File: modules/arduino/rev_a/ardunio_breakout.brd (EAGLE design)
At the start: 68.6 x 66 mm, 2 parts, among them J1 MODULE_GENERIC, U1 ARDUINO_SHIELDLABEL

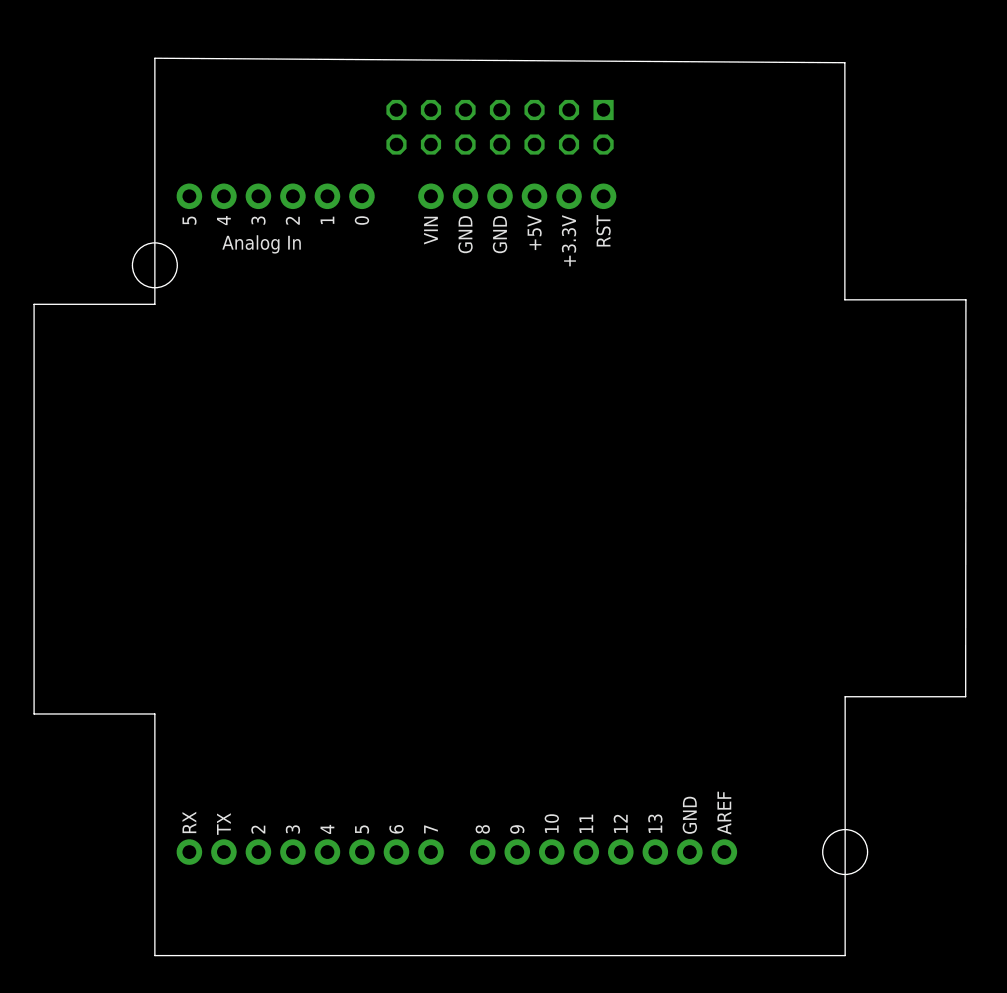
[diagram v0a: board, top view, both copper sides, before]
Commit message: Arduino Module: Regulator and headers
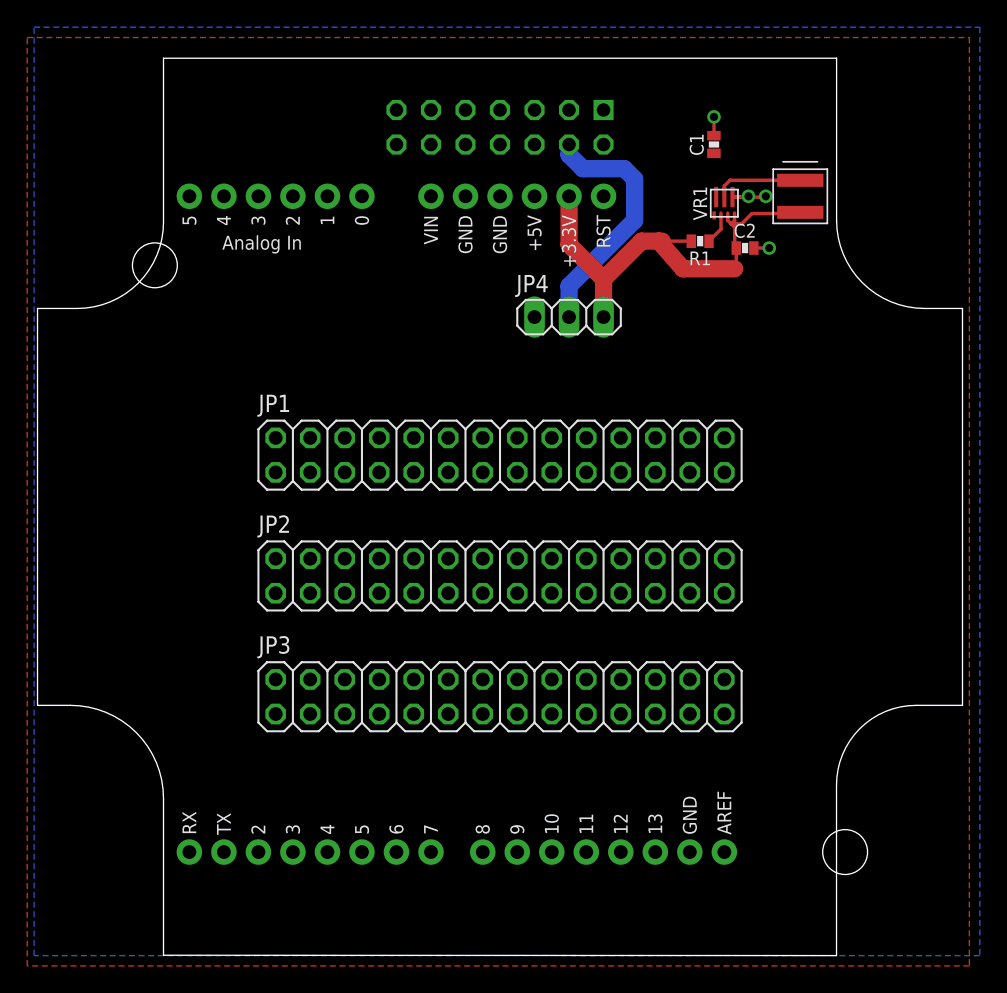
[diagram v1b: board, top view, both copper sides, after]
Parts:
- added C1: 10uF, passives:0603_CAP
- added C2: 22uF, passives:0603_CAP
- added JP1, JP2, JP3: (no value), pinhead:2X14
- added JP4: (no value), pinhead:1X03
- added L1: 0.47uH, passives:XFL4015
- added R1: 1MΩ, passives:0603-RES
- added VR1: TPS62086, regulators:RLT0007A
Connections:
- new net 3.3V: C2.1, JP4.3, L1.2, R1.2, U1.3.3V, VR1.3, VR1.4
- new net 5V: C1.1, J1.2, JP4.1, U1.5V, VR1.1, VR1.7
- new net D0: JP1.2, JP2.2, JP3.2, U1.RX
- new net D1: JP1.4, JP2.4, JP3.4, U1.TX
- new net D10: JP1.22, JP2.22, JP3.22, U1.D10
- new net D11: JP1.24, JP2.24, JP3.24, U1.D11
- new net D12: JP1.26, JP2.26, JP3.26, U1.D12
- new net D13: JP1.28, JP2.28, JP3.28, U1.D13
- new net D2: JP1.6, JP2.6, JP3.6, U1.D2
- new net D3: JP1.8, JP2.8, JP3.8, U1.D3
- new net D4: JP1.10, JP2.10, JP3.10, U1.D4
- new net D5: JP1.12, JP2.12, JP3.12, U1.D5
- new net D6: JP1.14, JP2.14, JP3.14, U1.D6
- new net D7: JP1.16, JP2.16, JP3.16, U1.D7
- new net D8: JP1.18, JP2.18, JP3.18, U1.D8
- new net D9: JP1.20, JP2.20, JP3.20, U1.D9
- new net MOD_IN: J1.10, JP2.1
- new net MOD_OUT: J1.8, JP1.1, JP1.11, JP1.13, JP1.15, JP1.17, JP1.19, JP1.21, JP1.23, JP1.25, JP1.27, JP1.3, JP1.5, JP1.7, JP1.9
- new net N$1: L1.1, VR1.6
- new net POWER_GOOD: R1.1, VR1.2
- new net PPS: J1.7, JP3.1
- new net SCL: J1.5, U1.A5
- new net SDA: J1.6, U1.A4
- new net VCCIO: J1.4, JP4.2
- net GND: now also C1.2, C2.2, VR1.5
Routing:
- net 3.3V: track 0.00 -> 34.5 mm
- net VCCIO: track 0.00 -> 18.5 mm
- net N$1: track 0.00 -> 6.58 mm
- net GND: track 0.00 -> 6.18 mm, vias 0 -> 4
- net POWER_GOOD: track 0.00 -> 2.26 mm
- added copper zone on layer 1, net 5V
- added copper zone on layer 16, net GND
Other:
- board size 68.6 x 66 mm -> 68.1 x 66 mm
